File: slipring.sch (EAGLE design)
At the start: 34 parts

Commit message: Add files via upload
Final version of gen1 boards, added initial cad of slipring with analog ground, switching to bourns connectors
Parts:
- removed AMP: AZV321, Diodes_Inc_By_element14_Batch_1:LMV321SEG-7
- removed C1: 2.2uF, Seeed-OPL-Capacitor:CERAMIC-0.5PF-50V-0.1PF-NPO(0603)
- removed C10, C4, C8: 100nF, Seeed-OPL-Capacitor:CERAMIC-0.5PF-50V-0.1PF-NPO(0603)
- removed C11, C3, C7: 10uF, Seeed-OPL-Capacitor:CERAMIC-0.5PF-50V-0.1PF-NPO(0603)
- removed C12, C9: 100nF, Seeed-OPL-Capacitor:CERAMIC-1PF-50V-0.25PF-NPO(0603)
- removed C2: 22uF, Seeed-OPL-Capacitor:CERAMIC-0.5PF-50V-0.1PF-NPO(0603)
- removed C5: 10pF, Seeed-OPL-Capacitor:CERAMIC-0.5PF-50V-0.1PF-NPO(0603)
- removed C6: 15pF, Seeed-OPL-Capacitor:CERAMIC-0.5PF-50V-0.1PF-NPO(0603)
- removed CLK: FXO_HC73, CUSTOM:FXO_HC73
- removed D1: B130-13-F, CUSTOM:B130-13-F
- removed DRIVER: TB6593FNG, CUSTOM:TB6593FNG
- removed ESP12: (no value), adafruit:ESP-12
- removed KEY: PTS645, CUSTOM:BUTTON
- removed L1: DFE252012C, CUSTOM:DFE252012C
- removed R10: 100k, resistor:R-US_R0603
- removed R2, R3, R4, R5: 10k, resistor:R-US_R0603
- removed R6, R7: 470, resistor:R-US_R0603
- removed R8: 1k, resistor:R-US_R0603
- removed R9: 33k, resistor:R-US_R0603
- removed SW: RN1906FE, CUSTOM:RN1906FE
- removed UART: CH340G, CUSTOM:CH340G
- removed USB: (no value), MicroUSB:USB""
- added U$2: RING3, CUSTOM:RING3
- CONN: value AVX_CONN -> BOURNS_2PIN; device CUSTOM:AVX_CONN -> CUSTOM:BOURNS_2PIN
- R1: value 1k -> 67
- REG: value TPS62177 -> LM334MX; device CUSTOM:TPS62177 -> CUSTOM:LM334MX
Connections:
- removed net +3V3: AMP.V+, C10.2, C11.2, C2.2, C3.2, C4.2, C5.1, C8.2, CLK.VDD, DRIVER.VCC, ESP12.VCC, L1.P$2, R1.1, R10.2, R2.1, R3.1, R4.1, REG.SLEEP, REG.VOS, UART.V3, UART.VCC
- removed net ADC: AMP.OUT, ESP12.ADC, R9.2
- removed net D+: UART.UD+, USB.D+
- removed net D-: UART.UD-, USB.D-
- removed net DTR: SW.B2, SW.E1, UART.DTR
- removed net EN: C12.2, ESP12.CH_PD, R1.2
- removed net GP0: ESP12.GPIO0, R3.2, SW.C1
- removed net GP14: ESP12.GPIO14
- removed net GP15: ESP12.GPIO15, R5.2
- removed net GP16: ESP12.GPIO16
- removed net GP2: ESP12.GPIO2, R4.2
- removed net IN1: DRIVER.IN1, ESP12.GPIO13
- removed net IN2: DRIVER.IN2, ESP12.GPIO12
- removed net M1: DRIVER.11, DRIVER.12
- removed net M2: DRIVER.21, DRIVER.22
- removed net N$1: R7.2, UART.TXD
- removed net N$2: R10.1, REG.PG
- removed net N$3: D1.AN, USB.VBUS
- removed net N$5: AMP.IN+, CONN.P2
- removed net N$6: AMP.IN-, R8.2, R9.1
- removed net N$7: R6.2, UART.RXD
- removed net PWM: DRIVER.PWM, ESP12.GPIO4
- removed net RST: C9.2, ESP12.RESET, KEY.1, R2.2, SW.C2
- removed net RTS: SW.B1, SW.E2, UART.RTS
- removed net RX: ESP12.RXD, R7.1
- removed net STBY: DRIVER.STBY, ESP12.GPIO5
- removed net SW: L1.P$1, REG.SW
- removed net TX: ESP12.TXD, R6.1
- removed net XI: C6.1, CLK.OUT, UART.XI
- new net AGND: U$2.AGND
- new net N$8: R1.2, REG.R
- new net N$9: R1.1, REG.V-, U$2.D
- net GND: now also CONN.P$2, U$2.GND; no longer AMP.V-, C1.1, C10.1, C11.1, C12.1, C2.1, C3.1, C4.1, C5.2, C6.2, C7.1, C8.1, C9.1, CLK.GND, CONN.P3, DRIVER.GND, DRIVER.PG1, DRIVER.PG2, DRIVER.PG3, DRIVER.PG4, DRIVER.PG5, DRIVER.PG6, ESP12.GND, KEY.3, R5.1, R8.1, REG.AGND, REG.FB, REG.NC, REG.PAD, REG.PGND, UART.GND, USB.G1, USB.G2, USB.G3, USB.G4, USB.G5, USB.G6, USB.GND
- net VCC: now also CONN.P$1, REG.V+, U$2.V+; no longer C1.2, C7.2, CONN.P1, D1.CATH, DRIVER.VM1, DRIVER.VM2, DRIVER.VM3, DRIVER.VM4, REG.EN, REG.VIN
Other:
- moved on the sheet: R1

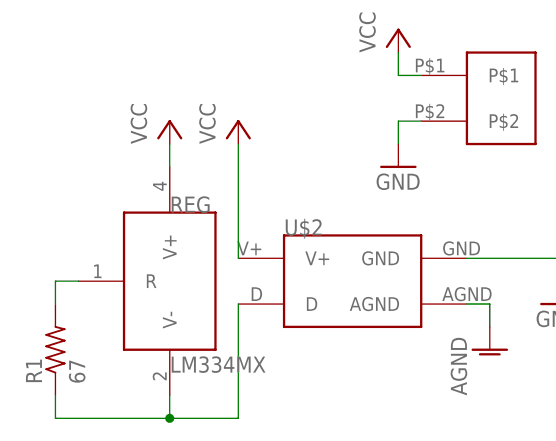
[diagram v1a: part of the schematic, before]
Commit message: switched to 20mA reg
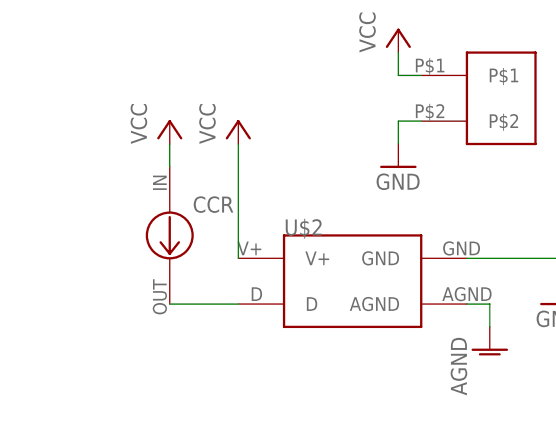
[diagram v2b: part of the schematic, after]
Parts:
- removed R1: 67, resistor:R-US_R0603
- removed REG: LM334MX, CUSTOM:LM334MX
- added CCR: CCR, CUSTOM:CCR
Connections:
- removed net N$8: R1.2, REG.R
- removed net N$9: R1.1, REG.V-, U$2.D
- new net N$3: CCR.OUT, U$2.D
- net VCC: now also CCR.IN; no longer REG.V+
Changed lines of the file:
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@@
 </classes>
 <parts>
-<part name="R1" library="resistor" deviceset="R-US_" device="R0603" value="67"/>
-<part name="REG" library="CUSTOM" deviceset="LM334MX" device=""/>
 <part name="P+5" library="supply1" deviceset="VCC" device=""/>
 <part name="P+6" library="supply1" deviceset="VCC" device=""/>
@@
 <part name="CONN" library="CUSTOM" deviceset="BOURNS_2PIN" device=""/>
 <part name="U$2" library="CUSTOM" deviceset="RING3" device=""/>
+<part name="CCR" library="CUSTOM" deviceset="CCR" device=""/>
 </parts>
 <sheets>
@@
 </plain>
 <instances>
-<instance part="R1" gate="G$1" x="25.4" y="27.94" rot="R90"/>
-<instance part="REG" gate="G$1" x="38.1" y="35.56"/>
 <instance part="P+5" gate="VCC" x="38.1" y="53.34"/>
 <instance part="P+6" gate="VCC" x="45.72" y="53.34"/>
@@
 <instance part="CONN" gate="G$1" x="73.66" y="55.88"/>
 <instance part="U$2" gate="G$1" x="58.42" y="38.1"/>
+<instance part="CCR" gate="G$1" x="38.1" y="40.64"/>
 </instances>
 <busses>
@@
 <segment>
 <pinref part="P+5" gate="VCC" pin="VCC"/>
-<pinref part="REG" gate="G$1" pin="V+"/>
 <wire x1="38.1" y1="50.8" x2="38.1" y2="48.26" width="0.1524" layer="91"/>
+<pinref part="CCR" gate="G$1" pin="IN"/>
 </segment>
 <segment>
@@
 </segment>
 </net>
-<net name="N$8" class="0">
-<segment>
-<pinref part="REG" gate="G$1" pin="R"/>
-<wire x1="27.94" y1="35.56" x2="25.4" y2="35.56" width="0.1524" layer="91"/>
-<pinref part="R1" gate="G$1" pin="2"/>
-<wire x1="25.4" y1="35.56" x2="25.4" y2="33.02" width="0.1524" layer="91"/>
-</segment>
-</net>
-<net name="N$9" class="0">
-<segment>
-<pinref part="R1" gate="G$1" pin="1"/>
-<wire x1="25.4" y1="22.86" x2="25.4" y2="20.32" width="0.1524" layer="91"/>
-<wire x1="25.4" y1="20.32" x2="38.1" y2="20.32" width="0.1524" layer="91"/>
-<pinref part="REG" gate="G$1" pin="V-"/>
-<wire x1="38.1" y1="22.86" x2="38.1" y2="20.32" width="0.1524" layer="91"/>
-<junction x="38.1" y="20.32"/>
-<wire x1="45.72" y1="20.32" x2="38.1" y2="20.32" width="0.1524" layer="91"/>
-<pinref part="U$2" gate="G$1" pin="D"/>
-<wire x1="45.72" y1="33.02" x2="45.72" y2="20.32" width="0.1524" layer="91"/>
-</segment>
-</net>
 <net name="AGND" class="0">
 <segment>
@@
 </segment>
 </net>
+<net name="N$3" class="0">
+<segment>
+<pinref part="U$2" gate="G$1" pin="D"/>
+<pinref part="CCR" gate="G$1" pin="OUT"/>
+<wire x1="45.72" y1="33.02" x2="38.1" y2="33.02" width="0.1524" layer="91"/>
+</segment>
+</net>

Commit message: final cad for purchase
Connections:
- net GND: now also CONN.P2; no longer CONN.P$2
- net VCC: now also CONN.P1; no longer CONN.P$1
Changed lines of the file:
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@@
 </segment>
 <segment>
-<pinref part="CONN" gate="G$1" pin="P$2"/>
+<pinref part="CONN" gate="G$1" pin="P2"/>
 <pinref part="GND25" gate="1" pin="GND"/>
 <wire x1="66.04" y1="53.34" x2="63.5" y2="53.34" width="0.1524" layer="91"/>
@@
 </segment>
 <segment>
-<pinref part="CONN" gate="G$1" pin="P$1"/>
+<pinref part="CONN" gate="G$1" pin="P1"/>
 <pinref part="P+7" gate="VCC" pin="VCC"/>
 <wire x1="66.04" y1="58.42" x2="63.5" y2="58.42" width="0.1524" layer="91"/>

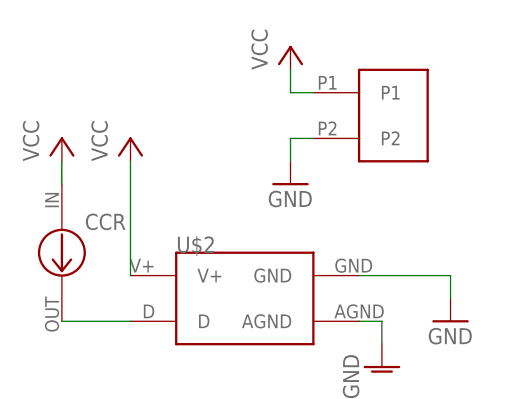
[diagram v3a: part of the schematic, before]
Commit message: fixed intial board errors, including short, flipped usb, and missing trace
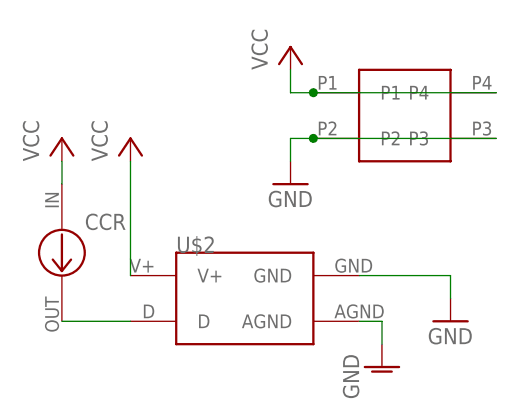
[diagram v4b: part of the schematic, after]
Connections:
- net GND: now also CONN.P3
- net VCC: now also CONN.P4
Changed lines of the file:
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@@
 <wire x1="66.04" y1="53.34" x2="63.5" y2="53.34" width="0.1524" layer="91"/>
 <wire x1="63.5" y1="53.34" x2="63.5" y2="50.8" width="0.1524" layer="91"/>
+<pinref part="CONN" gate="G$1" pin="P3"/>
+<wire x1="86.36" y1="53.34" x2="66.04" y2="53.34" width="0.1524" layer="91"/>
+<junction x="66.04" y="53.34"/>
 </segment>
 </net>
@@
 <wire x1="66.04" y1="58.42" x2="63.5" y2="58.42" width="0.1524" layer="91"/>
 <wire x1="63.5" y1="58.42" x2="63.5" y2="60.96" width="0.1524" layer="91"/>
+<pinref part="CONN" gate="G$1" pin="P4"/>
+<wire x1="66.04" y1="58.42" x2="86.36" y2="58.42" width="0.1524" layer="91"/>
+<junction x="66.04" y="58.42"/>
 </segment>
 </net>
